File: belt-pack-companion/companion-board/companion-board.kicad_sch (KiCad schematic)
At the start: 34 parts, among them J1 Conn_01x18_Socket, J2 Conn_01x18_Socket, J3 AudioJack4_Ground, J4 Micro_SD_Card, U1 TLV320AIC3204

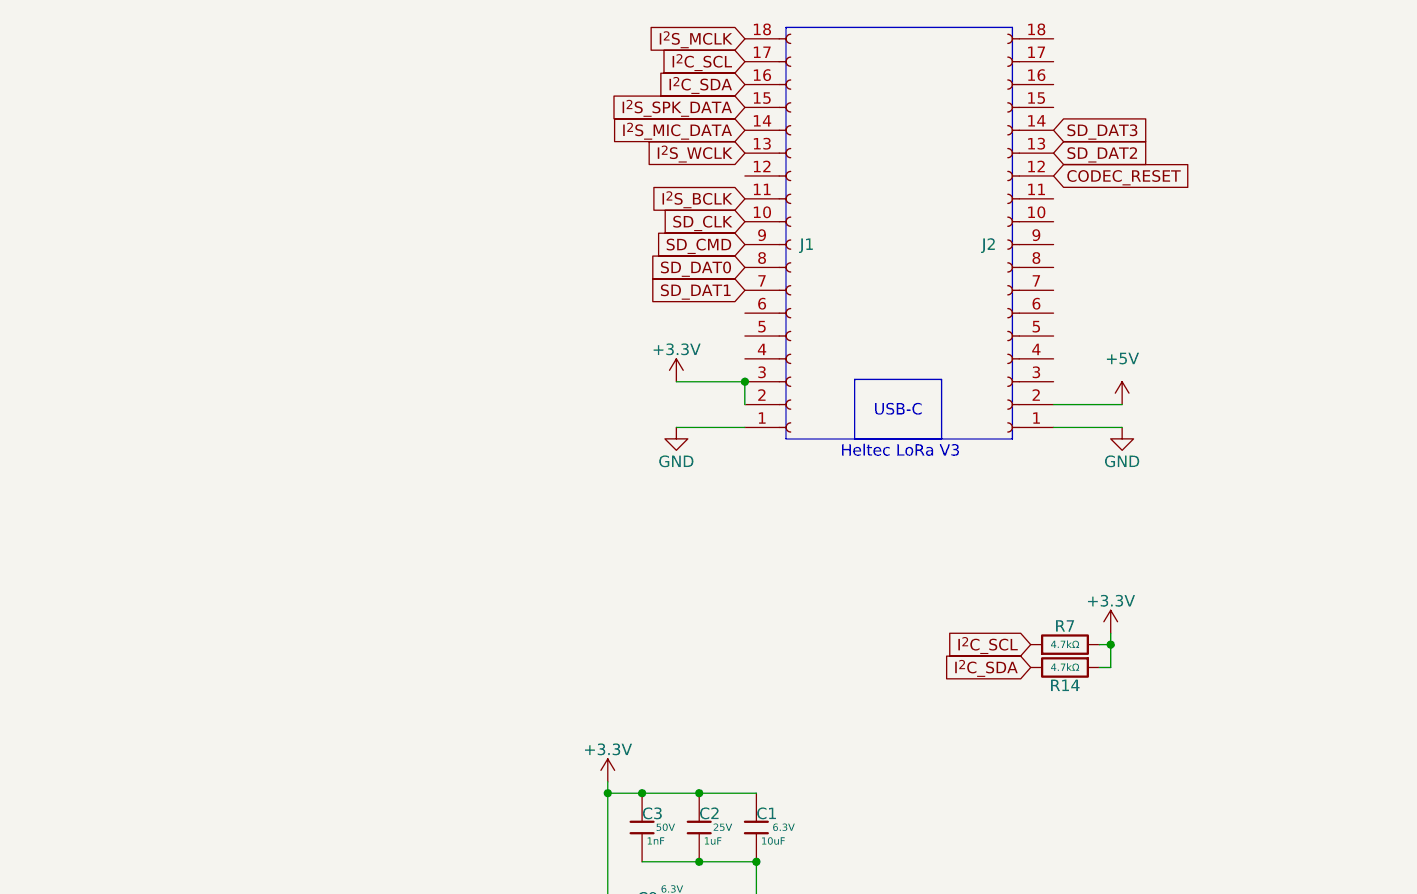
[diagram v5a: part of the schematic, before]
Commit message: Moved I2S MIC Data pin
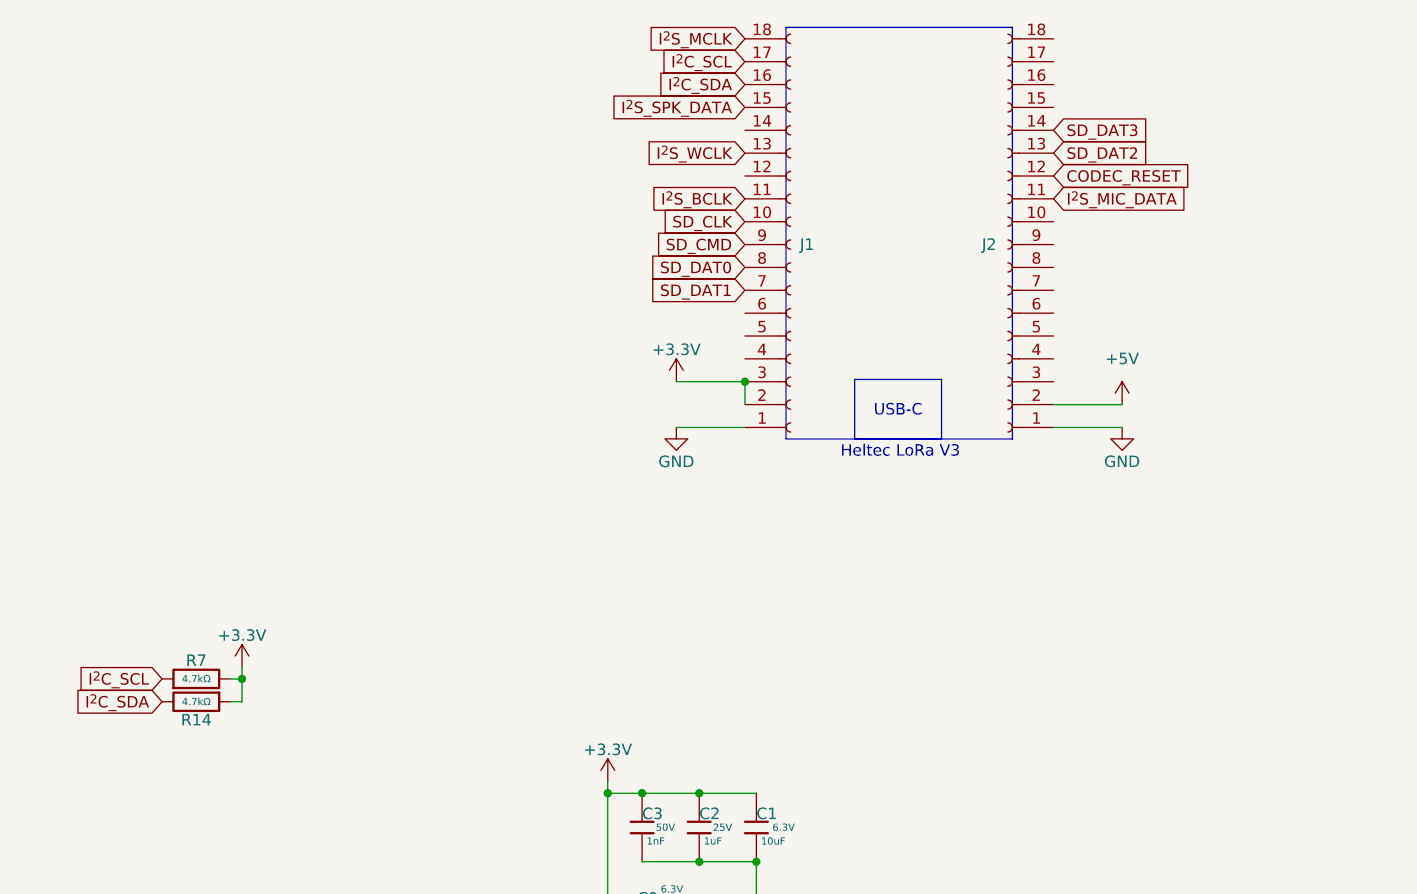
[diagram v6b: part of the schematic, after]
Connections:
- net I^{2}S_MIC_DATA: now also J2.11 (Pin_11); no longer J1.14 (Pin_14)
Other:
- moved on the sheet: R14, R7
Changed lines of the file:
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@@
 	)
 	(junction
-		(at 144.78 95.25)
+		(at 48.26 99.06)
 		(diameter 0)
 		(color 0 0 0 0)
@@
 	(wire
 		(pts
-			(xy 143.51 97.79) (xy 144.78 97.79)
+			(xy 46.99 101.6) (xy 48.26 101.6)
 		)
 		(stroke
@@
 	(wire
 		(pts
-			(xy 144.78 97.79) (xy 144.78 95.25)
+			(xy 48.26 101.6) (xy 48.26 99.06)
 		)
 		(stroke
@@
 	(wire
 		(pts
-			(xy 144.78 95.25) (xy 143.51 95.25)
+			(xy 48.26 99.06) (xy 46.99 99.06)
 		)
 		(stroke
@@
 	(wire
 		(pts
-			(xy 144.78 93.98) (xy 144.78 95.25)
+			(xy 48.26 97.79) (xy 48.26 99.06)
 		)
 		(stroke
@@
 	(global_label "I^{2}C_SCL"
 		(shape input)
-		(at 135.89 95.25 180)
+		(at 39.37 99.06 180)
 		(fields_autoplaced yes)
 		(effects
@@
 		)
 		(property "Intersheetrefs" "${INTERSHEET_REFS}"
-			(at 125.5872 95.25 0)
+			(at 29.0672 99.06 0)
 			(hide yes)
 			(show_name no)
@@
 		)
 	)
+	(global_label "I^{2}S_MIC_DATA"
+		(shape input)
+		(at 138.43 45.72 0)
+		(fields_autoplaced yes)
+		(effects
+			(font
+				(size 1.27 1.27)
+			)
+			(justify left)
+		)
+		(property "Intersheetrefs" "${INTERSHEET_REFS}"
+			(at 153.8733 45.72 0)
+			(hide yes)
+			(show_name no)
+			(do_not_autoplace no)
+			(effects
+				(font
+					(size 1.27 1.27)
+				)
+				(justify left)
+			)
+		)
+	)
 	(global_label "SD_CLK"
 		(shape input)
@@
 		)
 	)
-	(global_label "I^{2}S_MIC_DATA"
-		(shape input)
-		(at 104.14 38.1 180)
-		(fields_autoplaced yes)
-		(effects
-			(font
-				(size 1.27 1.27)
-			)
-			(justify right)
-		)
-		(property "Intersheetrefs" "${INTERSHEET_REFS}"
-			(at 88.6967 38.1 0)
-			(hide yes)
-			(show_name no)
-			(do_not_autoplace no)
-			(effects
-				(font
-					(size 1.27 1.27)
-				)
-				(justify right)
-			)
-		)
-	)
 	(global_label "I^{2}C_SDA"
 		(shape input)
-		(at 135.89 97.79 180)
+		(at 39.37 101.6 180)
 		(fields_autoplaced yes)
 		(effects
@@
 		)
 		(property "Intersheetrefs" "${INTERSHEET_REFS}"
-			(at 125.5267 97.79 0)
+			(at 29.0067 101.6 0)
 			(hide yes)
 			(show_name no)
@@
 	(symbol
 		(lib_id "PCM_JLCPCB-Resistors:0402,4.7kΩ")
-		(at 139.7 95.25 90)
+		(at 43.18 99.06 90)
 		(unit 1)
 		(body_style 1)
@@
 		(dnp no)
 		(property "Reference" "R7"
-			(at 139.7 93.218 90)
+			(at 43.18 97.028 90)
 			(show_name no)
 			(do_not_autoplace no)
@@
 		)
 		(property "Value" "4.7kΩ"
-			(at 139.7 95.25 90)
+			(at 43.18 99.06 90)
 			(show_name no)
 			(do_not_autoplace yes)
@@
 		)
 		(property "Footprint" "PCM_JLCPCB:R_0402"
-			(at 139.7 97.028 90)
+			(at 43.18 100.838 90)
 			(hide yes)
 			(show_name no)
@@
 		)
 		(property "Datasheet" "https://www.lcsc.com/datasheet/lcsc_datasheet_2206010045_UNI-ROYAL-Uniroyal-Elec-0402WGF4701TCE_C25900.pdf"
-			(at 139.7 95.25 0)
+			(at 43.18 99.06 0)
 			(hide yes)
 			(show_name no)
@@
 		)
 		(property "Description" "-55°C~+155°C 4.7kΩ 50V 62.5mW Thick Film Resistor ±1% ±100ppm/°C 0402 Chip Resistor - Surface Mount ROHS"
-			(at 139.7 95.25 0)
+			(at 43.18 99.06 0)
 			(hide yes)
 			(show_name no)
@@
 		)
 		(property "LCSC" "C25900"
-			(at 139.7 95.25 0)
+			(at 43.18 99.06 0)
 			(hide yes)
 			(show_name no)
@@
 		)
 		(property "Stock" "4461386"
-			(at 139.7 95.25 0)
+			(at 43.18 99.06 0)
 			(hide yes)
 			(show_name no)
@@
 		)
 		(property "Price" "0.004USD"
-			(at 139.7 95.25 0)
+			(at 43.18 99.06 0)
 			(hide yes)
 			(show_name no)
@@
 		)
 		(property "Process" "SMT"
-			(at 139.7 95.25 0)
+			(at 43.18 99.06 0)
 			(hide yes)
 			(show_name no)
@@
 		)
 		(property "Minimum Qty" "20"
-			(at 139.7 95.25 0)
+			(at 43.18 99.06 0)
 			(hide yes)
 			(show_name no)
@@
 		)
 		(property "Attrition Qty" "10"
-			(at 139.7 95.25 0)
+			(at 43.18 99.06 0)
 			(hide yes)
 			(show_name no)
@@
 		)
 		(property "Class" "Basic Component"
-			(at 139.7 95.25 0)
+			(at 43.18 99.06 0)
 			(hide yes)
 			(show_name no)
@@
 		)
 		(property "Category" "Resistors,Chip Resistor - Surface Mount"
-			(at 139.7 95.25 0)
+			(at 43.18 99.06 0)
 			(hide yes)
 			(show_name no)
@@
 		)
 		(property "Manufacturer" "UNI-ROYAL(Uniroyal Elec)"
-			(at 139.7 95.25 0)
+			(at 43.18 99.06 0)
 			(hide yes)
 			(show_name no)
@@
 		)
 		(property "Part" "0402WGF4701TCE"
-			(at 139.7 95.25 0)
+			(at 43.18 99.06 0)
 			(hide yes)
 			(show_name no)
@@
 		)
 		(property "Resistance" "4.7kΩ"
-			(at 139.7 95.25 0)
+			(at 43.18 99.06 0)
 			(hide yes)
 			(show_name no)
@@
 		)
 		(property "Power(Watts)" "62.5mW"
-			(at 139.7 95.25 0)
+			(at 43.18 99.06 0)
 			(hide yes)
 			(show_name no)
@@
 		)
 		(property "Type" "Thick Film Resistors"
-			(at 139.7 95.25 0)
+			(at 43.18 99.06 0)
 			(hide yes)
 			(show_name no)
@@
 		)
 		(property "Overload Voltage (Max)" "50V"
-			(at 139.7 95.25 0)
+			(at 43.18 99.06 0)
 			(hide yes)
 			(show_name no)
@@
 		)
 		(property "Operating Temperature Range" "-55°C~+155°C"
-			(at 139.7 95.25 0)
+			(at 43.18 99.06 0)
 			(hide yes)
 			(show_name no)
@@
 		)
 		(property "Tolerance" "±1%"
-			(at 139.7 95.25 0)
+			(at 43.18 99.06 0)
 			(hide yes)
 			(show_name no)
@@
 		)
 		(property "Temperature Coefficient" "±100ppm/°C"
-			(at 139.7 95.25 0)
+			(at 43.18 99.06 0)
 			(hide yes)
 			(show_name no)
@@
 	(symbol
 		(lib_id "power:+3.3V")
-		(at 144.78 93.98 0)
+		(at 48.26 97.79 0)
 		(unit 1)
 		(body_style 1)
@@
 		(dnp no)
 		(property "Reference" "#PWR016"
-			(at 144.78 97.79 0)
+			(at 48.26 101.6 0)
 			(hide yes)
 			(show_name no)
@@
 		)
 		(property "Value" "+3.3V"
-			(at 144.78 90.424 0)
+			(at 48.26 94.234 0)
 			(show_name no)
 			(do_not_autoplace no)
@@
 		)
 		(property "Footprint" ""
-			(at 144.78 93.98 0)
+			(at 48.26 97.79 0)
 			(hide yes)
 			(show_name no)
@@
 		)
 		(property "Datasheet" ""
-			(at 144.78 93.98 0)
+			(at 48.26 97.79 0)
 			(hide yes)
 			(show_name no)
@@
 		)
 		(property "Description" "Power symbol creates a global label with name \"+3.3V\""
-			(at 144.78 93.98 0)
+			(at 48.26 97.79 0)
 			(hide yes)
 			(show_name no)
@@
 	(symbol
 		(lib_id "PCM_JLCPCB-Resistors:0402,4.7kΩ")
-		(at 139.7 97.79 270)
+		(at 43.18 101.6 270)
 		(unit 1)
 		(body_style 1)
@@
 		(dnp no)
 		(property "Reference" "R14"
-			(at 139.7 99.822 90)
+			(at 43.18 103.632 90)
 			(show_name no)
 			(do_not_autoplace no)
@@
 		)
 		(property "Value" "4.7kΩ"
-			(at 139.7 97.79 90)
+			(at 43.18 101.6 90)
 			(show_name no)
 			(do_not_autoplace yes)
@@
 		)
 		(property "Footprint" "PCM_JLCPCB:R_0402"
-			(at 139.7 96.012 90)
+			(at 43.18 99.822 90)
 			(hide yes)
 			(show_name no)
@@
 		)
 		(property "Datasheet" "https://www.lcsc.com/datasheet/lcsc_datasheet_2206010045_UNI-ROYAL-Uniroyal-Elec-0402WGF4701TCE_C25900.pdf"
-			(at 139.7 97.79 0)
+			(at 43.18 101.6 0)
 			(hide yes)
 			(show_name no)
@@
 		)
 		(property "Description" "-55°C~+155°C 4.7kΩ 50V 62.5mW Thick Film Resistor ±1% ±100ppm/°C 0402 Chip Resistor - Surface Mount ROHS"
-			(at 139.7 97.79 0)
+			(at 43.18 101.6 0)
 			(hide yes)
 			(show_name no)
@@
 		)
 		(property "LCSC" "C25900"
-			(at 139.7 97.79 0)
+			(at 43.18 101.6 0)
 			(hide yes)
 			(show_name no)
@@
 		)
 		(property "Stock" "4461386"
-			(at 139.7 97.79 0)
+			(at 43.18 101.6 0)
 			(hide yes)
 			(show_name no)
@@
 		)
 		(property "Price" "0.004USD"
-			(at 139.7 97.79 0)
+			(at 43.18 101.6 0)
 			(hide yes)
 			(show_name no)
@@
 		)
 		(property "Process" "SMT"
-			(at 139.7 97.79 0)
+			(at 43.18 101.6 0)
 			(hide yes)
 			(show_name no)
@@
 		)
 		(property "Minimum Qty" "20"
-			(at 139.7 97.79 0)
+			(at 43.18 101.6 0)
 			(hide yes)
 			(show_name no)
@@
 		)
 		(property "Attrition Qty" "10"
-			(at 139.7 97.79 0)
+			(at 43.18 101.6 0)
 			(hide yes)
 			(show_name no)
@@
 		)
 		(property "Class" "Basic Component"
-			(at 139.7 97.79 0)
+			(at 43.18 101.6 0)
 			(hide yes)
 			(show_name no)
@@
 		)
 		(property "Category" "Resistors,Chip Resistor - Surface Mount"
-			(at 139.7 97.79 0)
+			(at 43.18 101.6 0)
 			(hide yes)
 			(show_name no)
@@
 		)
 		(property "Manufacturer" "UNI-ROYAL(Uniroyal Elec)"
-			(at 139.7 97.79 0)
+			(at 43.18 101.6 0)
 			(hide yes)
 			(show_name no)
@@
 		)
 		(property "Part" "0402WGF4701TCE"
-			(at 139.7 97.79 0)
+			(at 43.18 101.6 0)
 			(hide yes)
 			(show_name no)
@@
 		)
 		(property "Resistance" "4.7kΩ"
-			(at 139.7 97.79 0)
+			(at 43.18 101.6 0)
 			(hide yes)
 			(show_name no)
@@
 		)
 		(property "Power(Watts)" "62.5mW"
-			(at 139.7 97.79 0)
+			(at 43.18 101.6 0)
 			(hide yes)
 			(show_name no)
@@
 		)
 		(property "Type" "Thick Film Resistors"
-			(at 139.7 97.79 0)
+			(at 43.18 101.6 0)
 			(hide yes)
 			(show_name no)
@@
 		)
 		(property "Overload Voltage (Max)" "50V"
-			(at 139.7 97.79 0)
+			(at 43.18 101.6 0)
 			(hide yes)
 			(show_name no)
@@
 		)
 		(property "Operating Temperature Range" "-55°C~+155°C"
-			(at 139.7 97.79 0)
+			(at 43.18 101.6 0)
 			(hide yes)
 			(show_name no)
@@
 		)
 		(property "Tolerance" "±1%"
-			(at 139.7 97.79 0)
+			(at 43.18 101.6 0)
 			(hide yes)
 			(show_name no)
@@
 		)
 		(property "Temperature Coefficient" "±100ppm/°C"
-			(at 139.7 97.79 0)
+			(at 43.18 101.6 0)
 			(hide yes)
 			(show_name no)

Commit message: Schematic Progress
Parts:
- added R15, R16: 10kΩ, PCM_JLCPCB:R_0402, symbol PCM_JLCPCB-Resistors:0402,10kΩ
- added R17, R18: 470Ω, PCM_JLCPCB:R_0402, symbol PCM_JLCPCB-Resistors:0402,470Ω
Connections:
- net +3.3V: now also R15.2, R16.2
- net GND: now also D1.1, D4.1, S1.2 (B), S2.2 (B)
- net Button_2: now reaches J2.17 (Pin_17)
- net Button_2: now also S1.1 (A), R16.1
- net Button_1: now reaches J2.18 (Pin_18)
- net Button_1: now also S2.1 (A), R15.1
- net at D4.2: now also R17.2
- net at D1.2: now also R18.2
- net LED_Green: now reaches J1.5 (Pin_5)
- net LED_Green: now also R17.1
- net LED_Red: now reaches J1.6 (Pin_6)
- net LED_Red: now also R18.1
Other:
- moved on the sheet: D1, D2, D4, S1, S2
